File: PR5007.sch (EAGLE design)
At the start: 48 parts

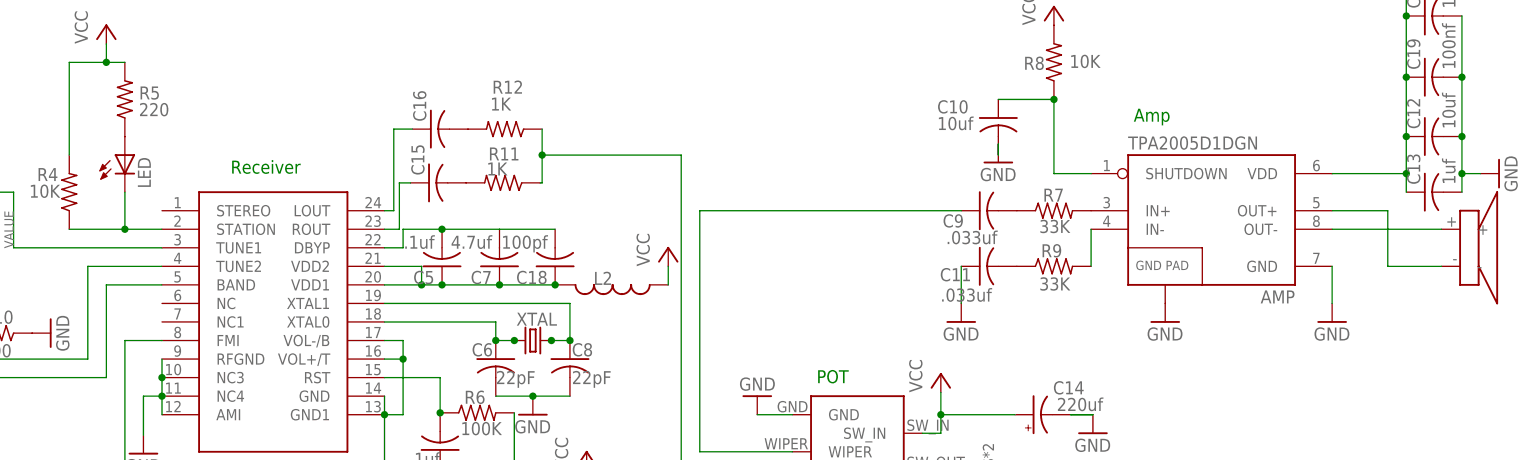
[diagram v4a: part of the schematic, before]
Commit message: Misc wishlist edits
made LED thru hole.
added restrict on battery clips
moved vcc traces to top layer to avoid bottom ground plane at battery
clips
misc re-routing chages
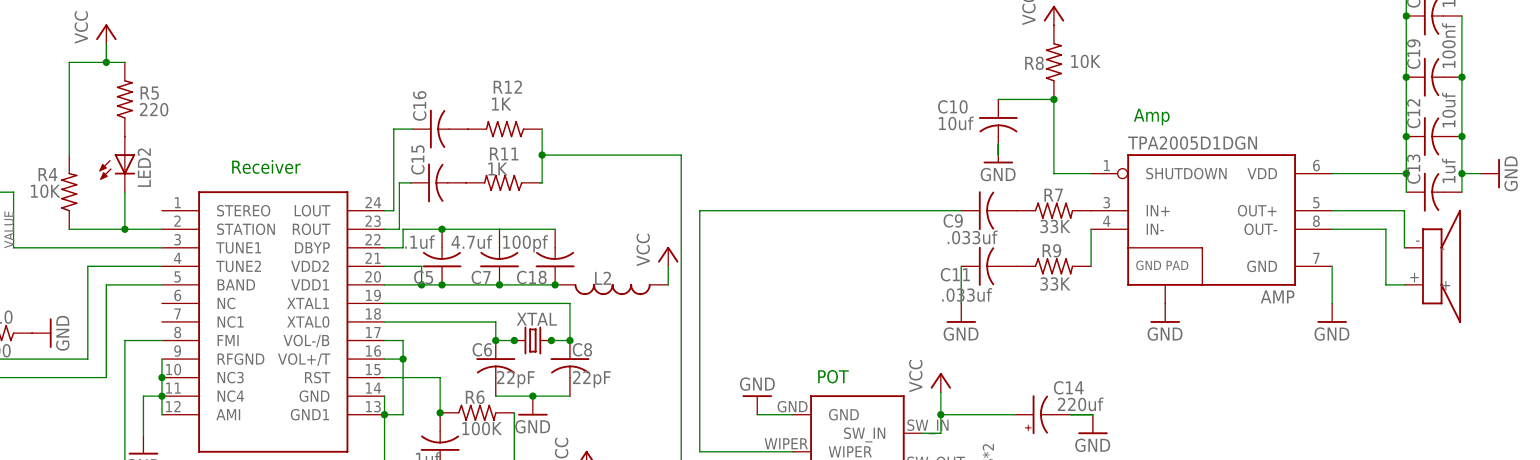
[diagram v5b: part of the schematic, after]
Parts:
- removed LED: (no value), adafruit:LEDCHIP-LED0603
- added LED2: (no value), SparkFun-LED:LED3MM
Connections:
- net N$11: now also LED2.A; no longer LED.A
- net N$9: now also LED2.C; no longer LED.C
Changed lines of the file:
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@@
 <?xml version="1.0" encoding="utf-8"?>
 <!DOCTYPE eagle SYSTEM "eagle.dtd">
-<eagle version="6.4">
+<eagle version="6.5.0">
 <drawing>
 <settings>
@@
 <setting verticaltext="up"/>
 </settings>
-<grid distance="0.01" unitdist="inch" unit="inch" style="lines" multiple="1" display="no" altdistance="0.01" altunitdist="inch" altunit="inch"/>
+<grid distance="0.1" unitdist="inch" unit="inch" style="lines" multiple="1" display="no" altdistance="0.01" altunitdist="inch" altunit="inch"/>
 <layers>
 <layer number="1" name="Top" color="4" fill="1" visible="no" active="no"/>
@@
 <part name="C4" library="resistor" deviceset="C-US" device="C0603" value=".1uf"/>
 <part name="R4" library="resistor" deviceset="R-US_" device="R0603" value="10K"/>
-<part name="LED" library="adafruit" deviceset="LED" device="CHIP-LED0603"/>
 <part name="R5" library="resistor" deviceset="R-US_" device="R0603" value="220"/>
 <part name="P+1" library="supply1" deviceset="VCC" device=""/>
@@
 <part name="GND14" library="SparkFun-Aesthetics" deviceset="GND" device=""/>
 <part name="P+6" library="supply1" deviceset="VCC" device=""/>
-<part name="U$3" library="PR_Libraries" deviceset="CE32A_DAYTON_SPKR" device=""/>
 <part name="ANT" library="PR_Libraries" deviceset="M3_SCREW_POST" device=""/>
 <part name="U$5" library="PR_Libraries" deviceset="P170_BOURNS_POT_SW" device=""/>
@@
 <part name="C19" library="resistor" deviceset="C-US" device="C0603" value="100nf"/>
 <part name="C20" library="resistor" deviceset="C-US" device="C0603" value="100pf"/>
+<part name="U$3" library="PR_Libraries" deviceset="CE32A_DAYTON_SPKR" device=""/>
+<part name="LED2" library="SparkFun-LED" deviceset="LED" device="3MM"/>
 </parts>
 <sheets>
@@
 <attribute name="VALUE" x="8.89" y="89.916" size="1.778" layer="96" rot="R180"/>
 </instance>
-<instance part="LED" gate="G$1" x="17.78" y="93.98"/>
 <instance part="R5" gate="G$1" x="17.78" y="101.6" smashed="yes" rot="R90">
 <attribute name="NAME" x="22.6314" y="103.378" size="1.778" layer="95" rot="R180"/>
@@
 <instance part="GND14" gate="1" x="137.16" y="22.86"/>
 <instance part="P+6" gate="VCC" x="129.54" y="64.008"/>
-<instance part="U$3" gate="G$1" x="200.66" y="81.28"/>
 <instance part="ANT" gate="G$1" x="-22.098" y="50.8" smashed="yes" rot="R90"/>
 <instance part="U$5" gate="G$1" x="116.84" y="53.34"/>
@@
 <instance part="C19" gate="G$1" x="195.834" y="104.648" rot="R90"/>
 <instance part="C20" gate="G$1" x="195.834" y="113.03" rot="R90"/>
+<instance part="U$3" gate="G$1" x="195.58" y="78.74" rot="MR180"/>
+<instance part="LED2" gate="G$1" x="17.78" y="93.98"/>
 </instances>
 <busses>
@@
 <pinref part="SI4831" gate="G$1" pin="STATION"/>
 <wire x1="10.16" y1="83.82" x2="17.78" y2="83.82" width="0.1524" layer="91"/>
-<pinref part="LED" gate="G$1" pin="C"/>
 <wire x1="17.78" y1="83.82" x2="22.86" y2="83.82" width="0.1524" layer="91"/>
 <wire x1="17.78" y1="88.9" x2="17.78" y2="83.82" width="0.1524" layer="91"/>
 <junction x="17.78" y="83.82"/>
-</segment>
-</net>
-<net name="N$11" class="0">
-<segment>
-<pinref part="LED" gate="G$1" pin="A"/>
-<pinref part="R5" gate="G$1" pin="1"/>
+<pinref part="LED2" gate="G$1" pin="C"/>
 </segment>
 </net>
@@
 </segment>
 </net>
-<net name="N$23" class="0">
-<segment>
-<pinref part="AMP" gate="G$1" pin="OUT+"/>
-<wire x1="190.754" y1="86.36" x2="183.134" y2="86.36" width="0.1524" layer="91"/>
-<wire x1="190.754" y1="86.36" x2="190.754" y2="78.74" width="0.1524" layer="91"/>
-<pinref part="U$3" gate="G$1" pin="-"/>
-<wire x1="190.754" y1="78.74" x2="198.12" y2="78.74" width="0.1524" layer="91"/>
-</segment>
-</net>
 <net name="N$32" class="0">
 <segment>
@@
 <net name="N$24" class="0">
 <segment>
+<pinref part="U$3" gate="G$1" pin="+"/>
+<wire x1="193.04" y1="76.2" x2="190.5" y2="76.2" width="0.1524" layer="91"/>
+<wire x1="190.5" y1="76.2" x2="190.5" y2="83.82" width="0.1524" layer="91"/>
 <pinref part="AMP" gate="G$1" pin="OUT-"/>
-<pinref part="U$3" gate="G$1" pin="+"/>
-<wire x1="183.134" y1="83.82" x2="198.12" y2="83.82" width="0.1524" layer="91"/>
-</segment>
-</net>
+<wire x1="183.134" y1="83.82" x2="190.5" y2="83.82" width="0.1524" layer="91"/>
+</segment>
+</net>
+<net name="N$23" class="0">
+<segment>
+<pinref part="U$3" gate="G$1" pin="-"/>
+<wire x1="193.04" y1="81.28" x2="193.04" y2="86.36" width="0.1524" layer="91"/>
+<pinref part="AMP" gate="G$1" pin="OUT+"/>
+<wire x1="193.04" y1="86.36" x2="183.134" y2="86.36" width="0.1524" layer="91"/>
+</segment>
+</net>
+<net name="N$11" class="0">
+<segment>
+<pinref part="R5" gate="G$1" pin="1"/>
+<pinref part="LED2" gate="G$1" pin="A"/>
+</segment>
+</net>

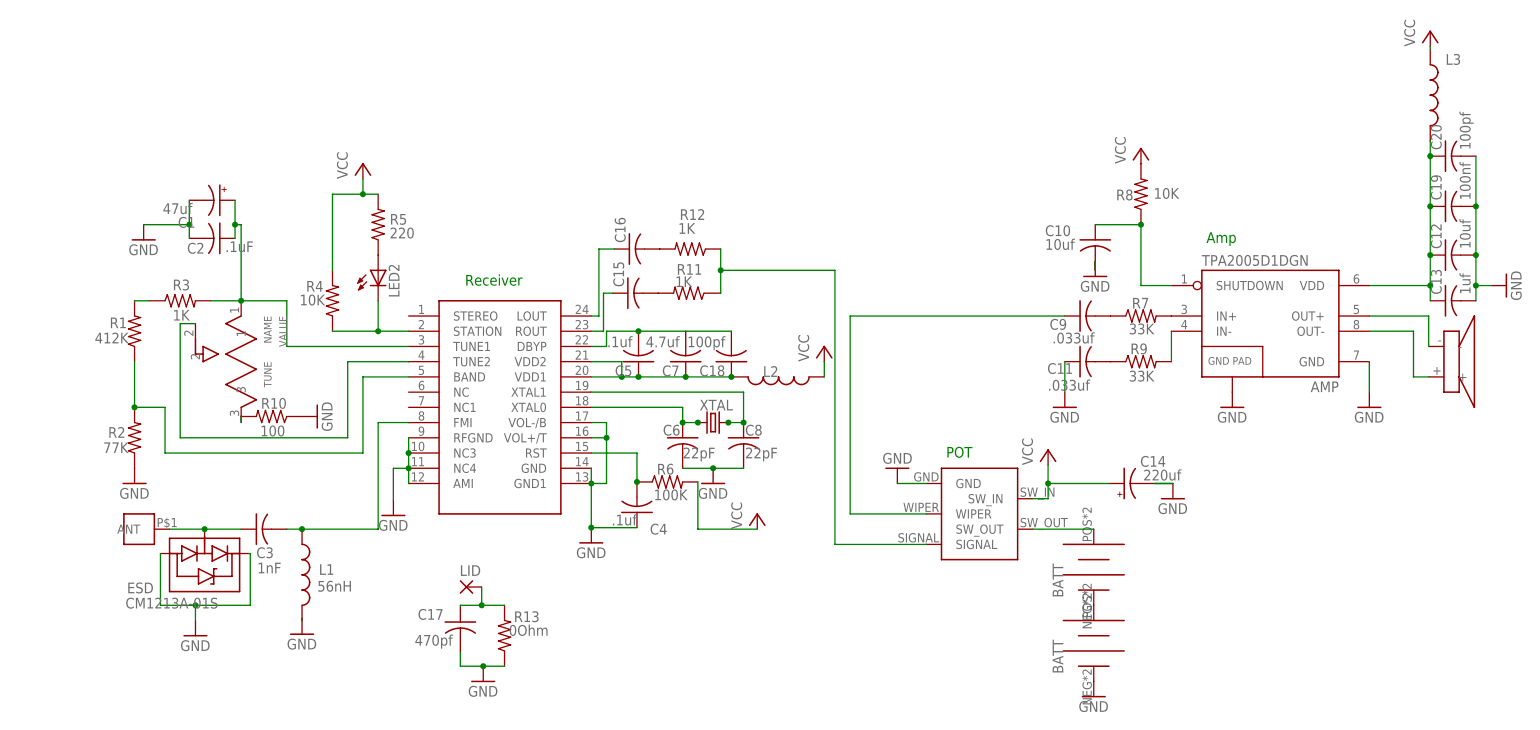
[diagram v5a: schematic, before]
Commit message: More Feature Request Updates
Added reverse polarity protection with p-channel mosfet, removed 1K
summing resistors for L&R mix, moved RF IC audio output to the bottom
layer, cleaned up part names and increased size for better print
resolution, added board # and station # markings on the bottom layer.
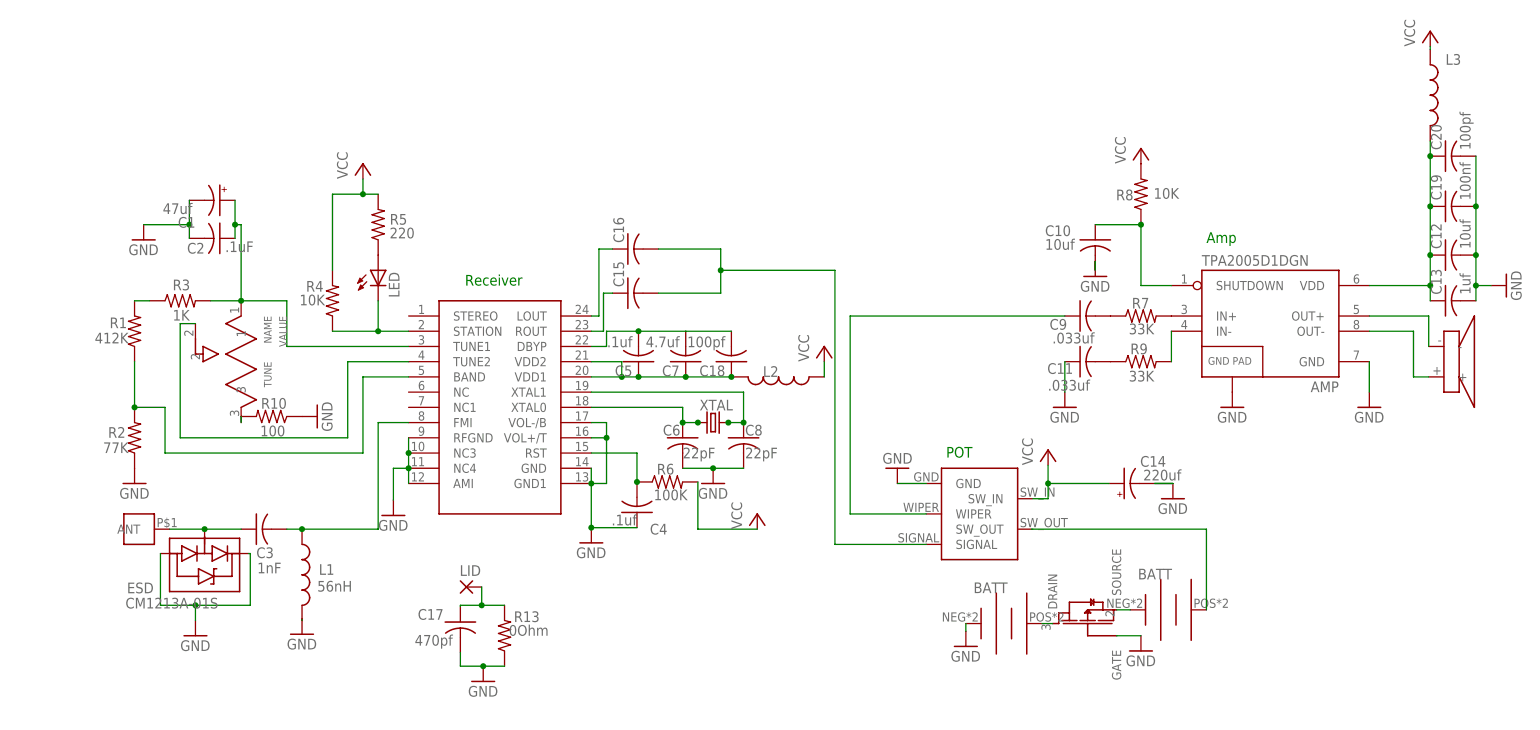
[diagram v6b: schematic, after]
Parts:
- removed R11, R12: 1K, resistor:R-US_R0603
- added REVPROTECT: SI2333DDS, PubRadioLib:SI2333DDS
- renumbered LED2 to LED
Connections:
- removed net N$32: U$1.POS, U$5.SW_OUT
- net GND: now also REVPROTECT.GATE
- net N$14: now also REVPROTECT.DRAIN; no longer U$1.NEG
- net N$21: now also REVPROTECT.SOURCE, U$1.NEG; no longer C15.2, R11.2
- net N$30: now also U$1.POS; no longer C16.2, R12.2
- net N$5: now also C15.2, C16.2; no longer R11.1, R12.1
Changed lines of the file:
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@@
 <?xml version="1.0" encoding="utf-8"?>
 <!DOCTYPE eagle SYSTEM "eagle.dtd">
-<eagle version="6.5.0">
+<eagle version="6.4">
 <drawing>
 <settings>
@@
 <setting verticaltext="up"/>
 </settings>
-<grid distance="0.1" unitdist="inch" unit="inch" style="lines" multiple="1" display="no" altdistance="0.01" altunitdist="inch" altunit="inch"/>
+<grid distance="0.01" unitdist="inch" unit="inch" style="lines" multiple="1" display="no" altdistance="0.01" altunitdist="inch" altunit="inch"/>
 <layers>
 <layer number="1" name="Top" color="4" fill="1" visible="no" active="no"/>
@@
 <part name="C15" library="resistor" deviceset="C-US" device="C0805"/>
 <part name="C16" library="resistor" deviceset="C-US" device="C0805"/>
-<part name="R11" library="resistor" deviceset="R-US_" device="R0603" value="1K"/>
-<part name="R12" library="resistor" deviceset="R-US_" device="R0603" value="1K"/>
 <part name="GND16" library="SparkFun-Aesthetics" deviceset="GND" device=""/>
 <part name="C17" library="resistor" deviceset="C-US" device="C0805" value="470pf"/>
@@
 <part name="C20" library="resistor" deviceset="C-US" device="C0603" value="100pf"/>
 <part name="U$3" library="PR_Libraries" deviceset="CE32A_DAYTON_SPKR" device=""/>
-<part name="LED2" library="SparkFun-LED" deviceset="LED" device="3MM"/>
+<part name="LED" library="SparkFun-LED" deviceset="LED" device="3MM"/>
+<part name="REVPROTECT" library="PubRadioLib" deviceset="SI2333DDS" device=""/>
+<part name="GND18" library="SparkFun-Aesthetics" deviceset="GND" device=""/>
 </parts>
 <sheets>
@@
 </instance>
 <instance part="GND13" gate="1" x="-21.336" y="99.06"/>
-<instance part="GND14" gate="1" x="137.16" y="22.86"/>
+<instance part="GND14" gate="1" x="115.824" y="31.242"/>
 <instance part="P+6" gate="VCC" x="129.54" y="64.008"/>
 <instance part="ANT" gate="G$1" x="-22.098" y="50.8" smashed="yes" rot="R90"/>
@@
 <attribute name="VALUE" x="2.286" y="68.072" size="1.778" layer="96" rot="R180"/>
 </instance>
-<instance part="U$1" gate="BATT" x="137.16" y="45.72" rot="R90"/>
-<instance part="U$2" gate="BATT" x="137.16" y="33.02" smashed="yes" rot="R90"/>
+<instance part="U$1" gate="BATT" x="150.876" y="37.338"/>
+<instance part="U$2" gate="BATT" x="123.444" y="35.052" smashed="yes"/>
 <instance part="C15" gate="G$1" x="59.436" y="90.17" rot="R90"/>
-<instance part="C16" gate="G$1" x="59.69" y="97.536" rot="R90"/>
-<instance part="R11" gate="G$1" x="69.596" y="90.17" smashed="yes" rot="R180">
-<attribute name="NAME" x="67.564" y="93.2434" size="1.778" layer="95"/>
-<attribute name="VALUE" x="67.31" y="91.186" size="1.778" layer="96"/>
-</instance>
-<instance part="R12" gate="G$1" x="69.85" y="97.536" smashed="yes" rot="R180">
-<attribute name="NAME" x="68.072" y="102.3874" size="1.778" layer="95"/>
-<attribute name="VALUE" x="67.818" y="100.076" size="1.778" layer="96"/>
-</instance>
+<instance part="C16" gate="G$1" x="59.436" y="97.536" rot="R90"/>
 <instance part="GND16" gate="1" x="150.368" y="55.88"/>
 <instance part="C17" gate="G$1" x="31.496" y="35.306" smashed="yes">
@@
 <instance part="C20" gate="G$1" x="195.834" y="113.03" rot="R90"/>
 <instance part="U$3" gate="G$1" x="195.58" y="78.74" rot="MR180"/>
-<instance part="LED2" gate="G$1" x="17.78" y="93.98"/>
+<instance part="LED" gate="G$1" x="17.78" y="93.98"/>
+<instance part="REVPROTECT" gate="G$1" x="136.144" y="35.56" rot="R90"/>
+<instance part="GND18" gate="1" x="145.034" y="30.48"/>
 </instances>
 <busses>
@@
 <pinref part="U$2" gate="BATT" pin="NEG"/>
 <pinref part="GND14" gate="1" pin="GND"/>
+<wire x1="115.824" y1="35.052" x2="115.824" y2="33.782" width="0.1524" layer="91"/>
 </segment>
 <segment>
@@
 <junction x="35.306" y="27.94"/>
 <pinref part="R13" gate="G$1" pin="1"/>
+</segment>
+<segment>
+<pinref part="REVPROTECT" gate="G$1" pin="GATE"/>
+<pinref part="GND18" gate="1" pin="GND"/>
+<wire x1="145.034" y1="33.02" x2="140.97" y2="33.02" width="0.1524" layer="91"/>
 </segment>
 </net>
@@
 <wire x1="17.78" y1="88.9" x2="17.78" y2="83.82" width="0.1524" layer="91"/>
 <junction x="17.78" y="83.82"/>
-<pinref part="LED2" gate="G$1" pin="C"/>
+<pinref part="LED" gate="G$1" pin="C"/>
 </segment>
 </net>
@@
 <wire x1="93.98" y1="48.26" x2="109.22" y2="48.26" width="0.1524" layer="91"/>
 <wire x1="74.93" y1="93.98" x2="93.98" y2="93.98" width="0.1524" layer="91"/>
-<pinref part="R12" gate="G$1" pin="1"/>
 <wire x1="74.93" y1="97.536" x2="74.93" y2="93.98" width="0.1524" layer="91"/>
-<pinref part="R11" gate="G$1" pin="1"/>
 <wire x1="74.93" y1="93.98" x2="74.93" y2="90.17" width="0.1524" layer="91"/>
-<wire x1="74.93" y1="90.17" x2="74.676" y2="90.17" width="0.1524" layer="91"/>
 <junction x="74.93" y="93.98"/>
+<pinref part="C15" gate="G$1" pin="2"/>
+<wire x1="64.516" y1="90.17" x2="74.93" y2="90.17" width="0.1524" layer="91"/>
+<wire x1="74.93" y1="97.536" x2="64.516" y2="97.536" width="0.1524" layer="91"/>
+<pinref part="C16" gate="G$1" pin="2"/>
 </segment>
 </net>
@@
 <pinref part="R10" gate="G$1" pin="2"/>
 <wire x1="-5.08" y1="69.596" x2="-5.08" y2="68.58" width="0.1524" layer="91"/>
-</segment>
-</net>
-<net name="N$14" class="0">
-<segment>
-<pinref part="U$1" gate="BATT" pin="NEG"/>
-<pinref part="U$2" gate="BATT" pin="POS"/>
-</segment>
-</net>
-<net name="N$32" class="0">
-<segment>
-<pinref part="U$5" gate="G$1" pin="SW_OUT"/>
-<wire x1="137.16" y1="50.8" x2="127" y2="50.8" width="0.1524" layer="91"/>
-<pinref part="U$1" gate="BATT" pin="POS"/>
 </segment>
 </net>
@@
 </segment>
 </net>
-<net name="N$21" class="0">
-<segment>
-<pinref part="C15" gate="G$1" pin="2"/>
-<pinref part="R11" gate="G$1" pin="2"/>
-</segment>
-</net>
-<net name="N$30" class="0">
-<segment>
-<pinref part="C16" gate="G$1" pin="2"/>
-<pinref part="R12" gate="G$1" pin="2"/>
-</segment>
-</net>
 <net name="N$31" class="0">
 <segment>
@@
 <wire x1="54.61" y1="86.36" x2="54.61" y2="97.536" width="0.1524" layer="91"/>
 <pinref part="C16" gate="G$1" pin="1"/>
-<wire x1="54.61" y1="97.536" x2="57.15" y2="97.536" width="0.1524" layer="91"/>
+<wire x1="54.61" y1="97.536" x2="56.896" y2="97.536" width="0.1524" layer="91"/>
 </segment>
 </net>
@@
 <segment>
 <pinref part="R5" gate="G$1" pin="1"/>
-<pinref part="LED2" gate="G$1" pin="A"/>
-</segment>
-</net>
+<pinref part="LED" gate="G$1" pin="A"/>
+</segment>
+</net>
+<net name="N$14" class="0">
+<segment>
+<pinref part="REVPROTECT" gate="G$1" pin="DRAIN"/>
+<wire x1="128.524" y1="35.052" x2="130.302" y2="35.052" width="0.1524" layer="91"/>
+<pinref part="U$2" gate="BATT" pin="POS"/>
+</segment>
+</net>
+<net name="N$21" class="0">
+<segment>
+<pinref part="REVPROTECT" gate="G$1" pin="SOURCE"/>
+<pinref part="U$1" gate="BATT" pin="NEG"/>
+<wire x1="140.97" y1="37.338" x2="143.256" y2="37.338" width="0.1524" layer="91"/>
+</segment>
+</net>
+<net name="N$30" class="0">
+<segment>
+<pinref part="U$1" gate="BATT" pin="POS"/>
+<wire x1="126.746" y1="50.8" x2="155.956" y2="50.8" width="0.1524" layer="91"/>
+<wire x1="155.956" y1="50.8" x2="155.956" y2="37.338" width="0.1524" layer="91"/>
+</segment>
+</net>
